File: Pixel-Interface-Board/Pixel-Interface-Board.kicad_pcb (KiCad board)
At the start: 2 copper layers, 29 parts, among them IC1 ATTINY85-P, P1 CONN_02X20, SW1 SW_PUSH, SW10 SW_PUSH, SW11 SW_PUSH, SW12 SW_PUSH, SW2 SW_PUSH, SW3 SW_PUSH, SW4 SW_PUSH, SW5 SW_PUSH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

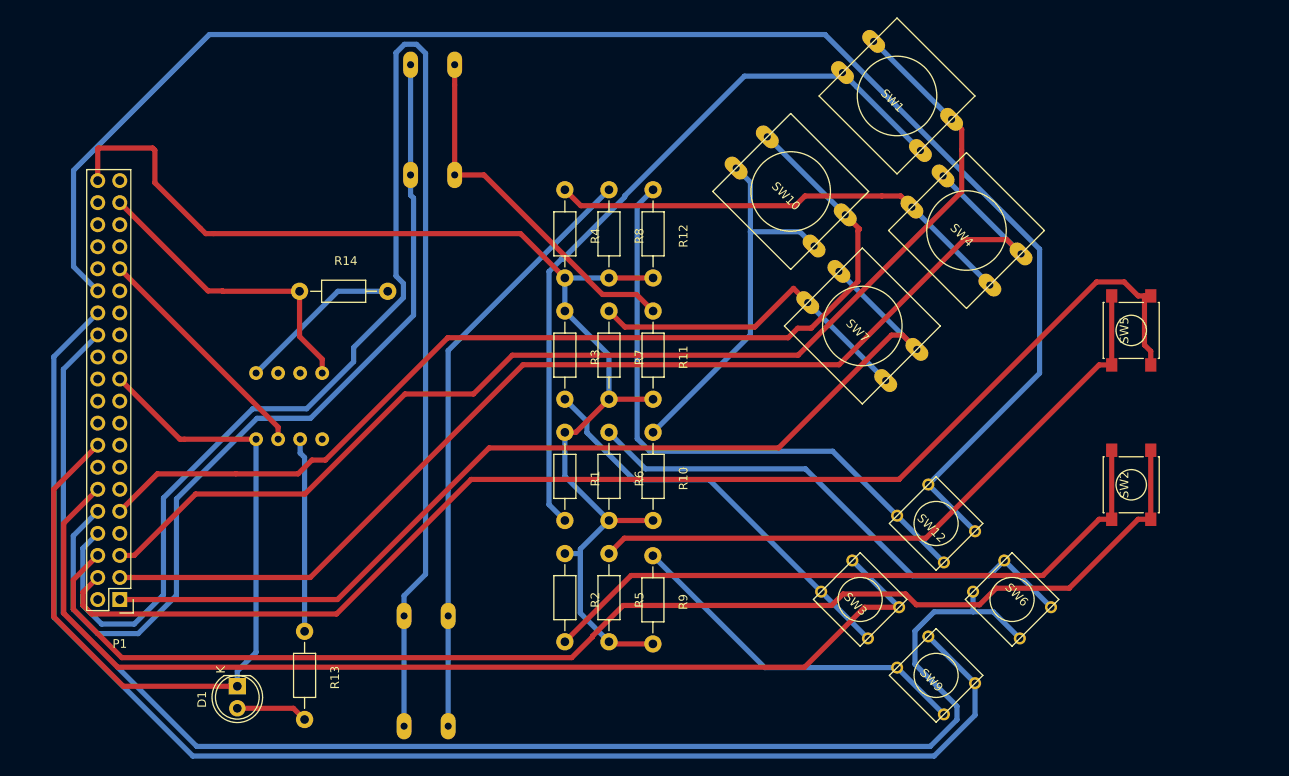
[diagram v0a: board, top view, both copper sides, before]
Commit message: Fixed the interface board, FINALLY.
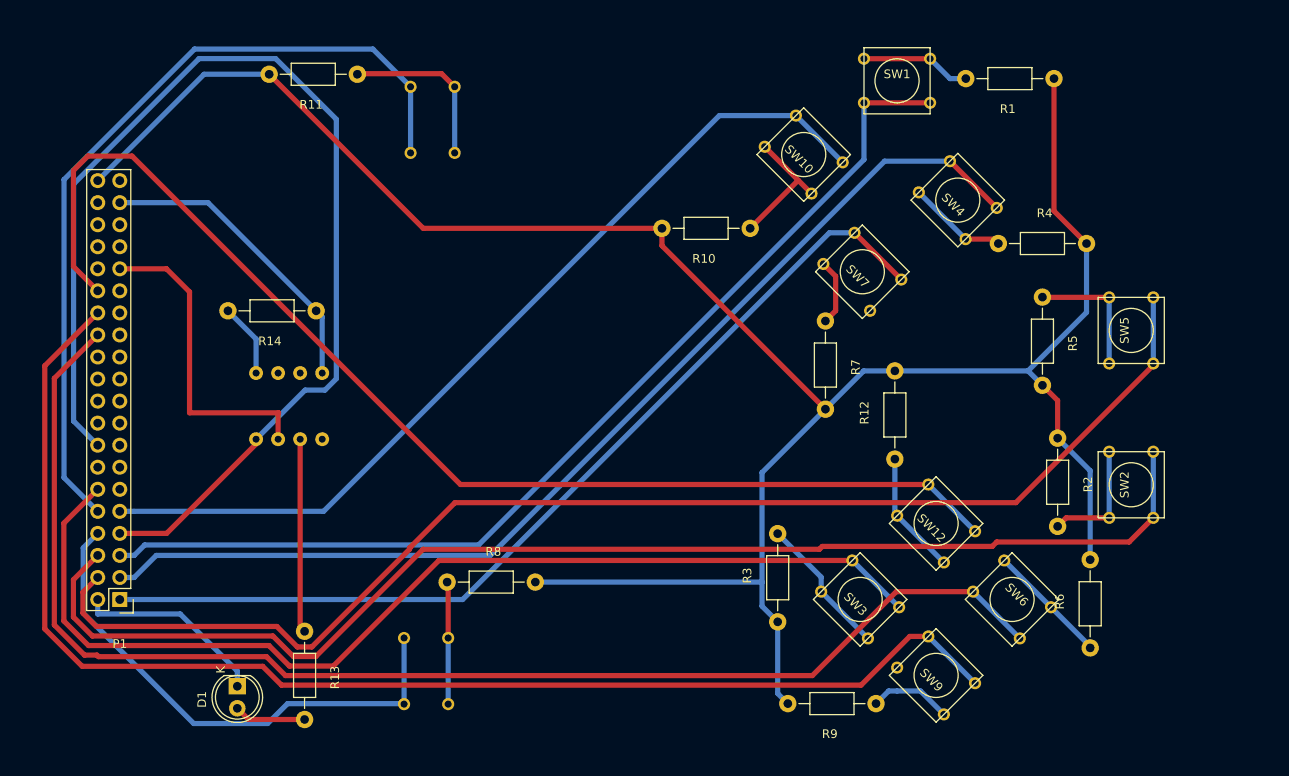
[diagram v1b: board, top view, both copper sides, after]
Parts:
- SW1, SW10, SW11, SW4, SW7, SW8: footprint Buttons_Switches_ThroughHole:SW_PUSH-12mm -> Buttons_Switches_ThroughHole:SW_PUSH_SMALL
- SW2, SW5: footprint Buttons_Switches_SMD:SW_SPST_PTS645 -> Buttons_Switches_ThroughHole:SW_PUSH_SMALL
- moved R1 68.8 mm to (127.8, 18.0), turned to 180 degrees
- moved R2 58.3 mm to (133.2, 64.5)
- moved R5 58.0 mm to (131.5, 48.2)
- moved R6 57.3 mm to (137.0, 78.5), turned to 90 degrees
- moved R4 55.0 mm to (131.5, 37.0), turned to 0 degrees
- moved R11 50.8 mm to (47.5, 17.5), turned to 180 degrees
- moved R8 42.3 mm to (68.0, 76.0), turned to 0 degrees
- moved R3 35.5 mm to (101.0, 75.5), turned to 90 degrees
- moved R12 34.8 mm to (114.5, 56.8), turned to 90 degrees
- moved R10 29.2 mm to (92.8, 35.2), turned to 180 degrees
- moved R7 25.0 mm to (106.5, 51.0)
- moved R9 23.8 mm to (107.2, 90.0), turned to 180 degrees
- moved R14 8.55 mm to (42.8, 44.8), turned to 180 degrees
- moved SW7 6.25 mm to (110.8, 40.2)
- moved SW10 4.51 mm to (104.0, 26.8)
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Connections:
- IC1 pad 1: Net-(IC1-Pad1) -> (no net)
- IC1 pad 6: Net-(IC1-Pad6) -> (no net)
- IC1 pad 7: /CHG_SW -> (no net)
- P1 pad 13: Net-(P1-Pad13) -> (no net)
- P1 pad 14: Net-(P1-Pad14) -> (no net)
- P1 pad 15: Net-(P1-Pad15) -> (no net)
- P1 pad 17: Net-(P1-Pad17) -> (no net)
- P1 pad 18: Net-(P1-Pad18) -> (no net)
- P1 pad 19: Net-(P1-Pad19) -> (no net)
- P1 pad 20: Net-(P1-Pad20) -> (no net)
- P1 pad 22: Net-(P1-Pad22) -> (no net)
- P1 pad 23: Net-(P1-Pad23) -> (no net)
- P1 pad 25: Net-(P1-Pad25) -> (no net)
- P1 pad 27: Net-(P1-Pad27) -> (no net)
- P1 pad 29: Net-(P1-Pad29) -> (no net)
- P1 pad 33: /UART_TX -> (no net)
- P1 pad 34: Net-(P1-Pad34) -> (no net)
- P1 pad 36: Net-(P1-Pad36) -> (no net)
- P1 pad 38: Net-(P1-Pad38) -> (no net)
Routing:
- net /L: track 181.2 -> 60.7 mm
- net VDD: track 144.9 -> 258.2 mm
- net Net-(R1-Pad2): track 85.8 -> 12.7 mm
- net Net-(R2-Pad2): track 76.8 -> 14.0 mm
- net GND: track 94.6 -> 155.1 mm
- net Net-(R5-Pad1): track 74.9 -> 15.3 mm
- net Net-(R12-Pad1): track 70.7 -> 14.2 mm
- net Net-(R8-Pad1): track 69.5 -> 14.1 mm
- net Net-(R6-Pad1): track 60.7 -> 14.2 mm
- net /RIGHT: track 183.1 -> 137.5 mm
- net Net-(R4-Pad1): track 54.4 -> 11.6 mm
- net Net-(R9-Pad1): track 41.1 -> 9.54 mm
- net Net-(R7-Pad1): track 38.9 -> 7.64 mm
- net Net-(R3-Pad2): track 47.1 -> 16.4 mm
- net Net-(R10-Pad1): track 43.8 -> 15.5 mm
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
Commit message: Fixed R trace to fit within OSHPark specs.  Unfortunately, a very long trace circling the entire board has resulted from this.
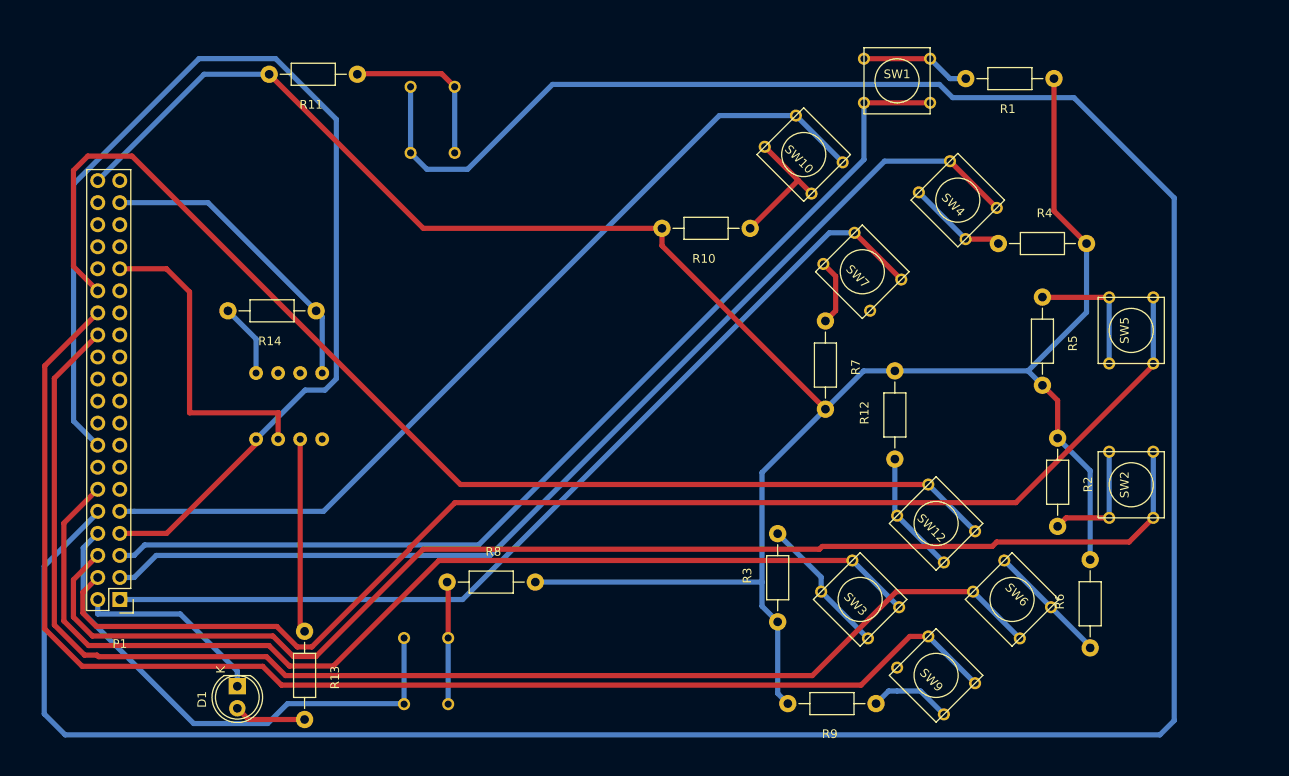
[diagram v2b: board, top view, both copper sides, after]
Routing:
- net /R: track 95.4 -> 323.8 mm
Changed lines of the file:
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@@
-(kicad_pcb (version 4) (host pcbnew 0.201509061501+6161~29~ubuntu14.04.1-product)
+(kicad_pcb (version 4) (host pcbnew "(2015-12-28 BZR 6407, Git 3dff6c0)-product")
   (general
     (links 76)
@@
     (thickness 1.6)
     (drawings 6)
-    (tracks 193)
+    (tracks 202)
     (zones 0)
     (modules 29)
@@
   (gr_line (start 153.5372 14.52) (end 13.5372 14.52) (layer Dwgs.User) (width 0.1))
   (gr_line (start 153.5372 94.52) (end 153.5372 14.52) (layer Dwgs.User) (width 0.1))
-  (segment (start 40.91 59.54) (end 40.91 60.09) (width 0.6) (layer F.Cu) (net 1) (status C00000))
-  (segment (start 40.91 60.09) (end 30.61 70.39) (width 0.6) (layer F.Cu) (net 1) (status 400000))
-  (segment (start 30.61 70.39) (end 25.21 70.39) (width 0.6) (layer F.Cu) (net 1) (status 800000))
+  (segment (start 40.91 59.54) (end 40.91 60.09) (width 0.6) (layer F.Cu) (net 1))
+  (segment (start 40.91 60.09) (end 30.61 70.39) (width 0.6) (layer F.Cu) (net 1))
+  (segment (start 30.61 70.39) (end 25.21 70.39) (width 0.6) (layer F.Cu) (net 1))
   (segment (start 32.1738 79.6737) (end 38.75 86.2499) (width 0.6) (layer B.Cu) (net 1))
   (segment (start 22.67 79.6737) (end 32.1738 79.6737) (width 0.6) (layer B.Cu) (net 1))
@@
   (segment (start 45.99 81.16) (end 45.99 59.54) (width 0.6) (layer F.Cu) (net 3))
   (segment (start 46.5 81.67) (end 45.99 81.16) (width 0.6) (layer F.Cu) (net 3))
-  (segment (start 25.21 39.91) (end 30.59 39.91) (width 0.6) (layer F.Cu) (net 4) (status 400000))
-  (segment (start 43.45 56.55) (end 43.45 59.54) (width 0.6) (layer F.Cu) (net 4) (status 800000))
+  (segment (start 25.21 39.91) (end 30.59 39.91) (width 0.6) (layer F.Cu) (net 4))
+  (segment (start 43.45 56.55) (end 43.45 59.54) (width 0.6) (layer F.Cu) (net 4))
   (segment (start 43.5 56.5) (end 43.45 56.55) (width 0.6) (layer F.Cu) (net 4))
   (segment (start 33.25 56.5) (end 43.5 56.5) (width 0.6) (layer F.Cu) (net 4))
@@
   (segment (start 94.28 22.2599) (end 48.6899 67.85) (width 0.6) (layer B.Cu) (net 13))
   (segment (start 103.102 22.2599) (end 94.28 22.2599) (width 0.6) (layer B.Cu) (net 13))
+  (segment (start 22.67 67.85) (end 22.67 68.008) (width 0.6) (layer B.Cu) (net 14) (status C00000))
+  (segment (start 22.67 68.008) (end 16.51 74.168) (width 0.6) (layer B.Cu) (net 14) (status 400000))
+  (segment (start 60.598 28.448) (end 58.71 26.56) (width 0.6) (layer B.Cu) (net 14) (status 800000))
+  (segment (start 65.278 28.448) (end 60.598 28.448) (width 0.6) (layer B.Cu) (net 14))
+  (segment (start 75.057 18.669) (end 65.278 28.448) (width 0.6) (layer B.Cu) (net 14))
+  (segment (start 119.634 18.669) (end 75.057 18.669) (width 0.6) (layer B.Cu) (net 14))
+  (segment (start 121.158 20.193) (end 119.634 18.669) (width 0.6) (layer B.Cu) (net 14))
+  (segment (start 135.128 20.193) (end 121.158 20.193) (width 0.6) (layer B.Cu) (net 14))
+  (segment (start 146.685 31.75) (end 135.128 20.193) (width 0.6) (layer B.Cu) (net 14))
+  (segment (start 146.685 91.948) (end 146.685 31.75) (width 0.6) (layer B.Cu) (net 14))
+  (segment (start 145.034 93.599) (end 146.685 91.948) (width 0.6) (layer B.Cu) (net 14))
+  (segment (start 18.923 93.599) (end 145.034 93.599) (width 0.6) (layer B.Cu) (net 14))
+  (segment (start 16.51 91.186) (end 18.923 93.599) (width 0.6) (layer B.Cu) (net 14))
+  (segment (start 16.51 74.168) (end 16.51 91.186) (width 0.6) (layer B.Cu) (net 14))
   (segment (start 58.71 26.56) (end 58.71 18.94) (width 0.6) (layer B.Cu) (net 14))
-  (segment (start 18.7875 63.9675) (end 22.67 67.85) (width 0.6) (layer B.Cu) (net 14))
-  (segment (start 18.7875 29.6337) (end 18.7875 63.9675) (width 0.6) (layer B.Cu) (net 14))
-  (segment (start 33.8241 14.5971) (end 18.7875 29.6337) (width 0.6) (layer B.Cu) (net 14))
-  (segment (start 54.3671 14.5971) (end 33.8241 14.5971) (width 0.6) (layer B.Cu) (net 14))
-  (segment (start 58.71 18.94) (end 54.3671 14.5971) (width 0.6) (layer B.Cu) (net 14))
   (segment (start 114.9901 78.898) (end 109.602 73.5099) (width 0.6) (layer B.Cu) (net 15))
   (segment (start 61.9709 73.5099) (end 109.602 73.5099) (width 0.6) (layer F.Cu) (net 15))

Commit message: Added board outline to the proper layer.
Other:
- board outline added: 140.2 x 80.3 mm
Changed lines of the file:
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@@
     (area 11 12 156 97)
     (thickness 1.6)
-    (drawings 6)
+    (drawings 8)
     (tracks 202)
     (zones 0)
@@
     (visible_elements FFFFF77F)
     (pcbplotparams
-      (layerselection 0x00130_80000001)
+      (layerselection 0x00130_ffffffff)
       (usegerberextensions false)
       (excludeedgelayer true)
@@
       (drillshape 0)
       (scaleselection 1)
-      (outputdirectory "Gerber Originals"))
+      (outputdirectory "Gerber Originals/"))
   )
   (net 0 "")
@@
       (net 14 /R))
   )
-  (target plus (at 153.5 14.5) (size 5) (width 0.1) (layer Edge.Cuts))
-  (target plus (at 13.5 94.5) (size 5) (width 0.1) (layer Edge.Cuts))
+  (gr_line (start 13.462 14.351) (end 13.462 94.615) (angle 90) (layer Edge.Cuts) (width 0.1))
+  (gr_line (start 153.67 14.351) (end 13.462 14.351) (angle 90) (layer Edge.Cuts) (width 0.1))
+  (gr_line (start 153.67 94.615) (end 153.67 14.351) (angle 90) (layer Edge.Cuts) (width 0.1))
+  (gr_line (start 13.462 94.615) (end 153.67 94.615) (angle 90) (layer Edge.Cuts) (width 0.1))
   (gr_line (start 13.5372 94.52) (end 153.5372 94.52) (layer Dwgs.User) (width 0.1))
   (gr_line (start 13.5372 14.52) (end 13.5372 94.52) (layer Dwgs.User) (width 0.1))
@@
   (segment (start 94.28 22.2599) (end 48.6899 67.85) (width 0.6) (layer B.Cu) (net 13))
   (segment (start 103.102 22.2599) (end 94.28 22.2599) (width 0.6) (layer B.Cu) (net 13))
-  (segment (start 22.67 67.85) (end 22.67 68.008) (width 0.6) (layer B.Cu) (net 14) (status C00000))
-  (segment (start 22.67 68.008) (end 16.51 74.168) (width 0.6) (layer B.Cu) (net 14) (status 400000))
-  (segment (start 60.598 28.448) (end 58.71 26.56) (width 0.6) (layer B.Cu) (net 14) (status 800000))
+  (segment (start 22.67 67.85) (end 22.67 68.008) (width 0.6) (layer B.Cu) (net 14))
+  (segment (start 22.67 68.008) (end 16.51 74.168) (width 0.6) (layer B.Cu) (net 14))
+  (segment (start 60.598 28.448) (end 58.71 26.56) (width 0.6) (layer B.Cu) (net 14))
   (segment (start 65.278 28.448) (end 60.598 28.448) (width 0.6) (layer B.Cu) (net 14))
   (segment (start 75.057 18.669) (end 65.278 28.448) (width 0.6) (layer B.Cu) (net 14))

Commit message: Oooh, silkscreen...
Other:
- board text added: "DMG-32"
- board text added: "Open Source Hardware and Software"
- board text added: "PyroAVR/DMG-32"
- board text added: "~Andy "PyroAVR" Meyer"
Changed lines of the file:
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@@
     (area 11 12 156 97)
     (thickness 1.6)
-    (drawings 8)
+    (drawings 12)
     (tracks 202)
     (zones 0)
@@
       (net 14 /R))
   )
+  (gr_text PyroAVR/DMG-32 (at 82.423 89.535) (layer F.SilkS)
+    (effects (font (size 1.5 1.5) (thickness 0.3)))
+  )
+  (gr_text "Open Source Hardware and Software" (at 83.312 91.821) (layer F.SilkS)
+    (effects (font (size 1.5 1.5) (thickness 0.3)))
+  )
+  (gr_text "~Andy \"PyroAVR\" Meyer" (at 140.843 15.748) (layer F.SilkS)
+    (effects (font (size 1.5 1.5) (thickness 0.3)))
+  )
+  (gr_text DMG-32 (at 78.994 47.879) (layer F.SilkS)
+    (effects (font (size 3 3) (thickness 0.3)))
+  )
   (gr_line (start 13.462 14.351) (end 13.462 94.615) (angle 90) (layer Edge.Cuts) (width 0.1))
